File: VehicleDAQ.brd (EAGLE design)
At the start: 100 x 80 mm, 15 parts, among them IC1 786TV, IC3 78L05Z, X1 RASPI_BOARD_B+_FP

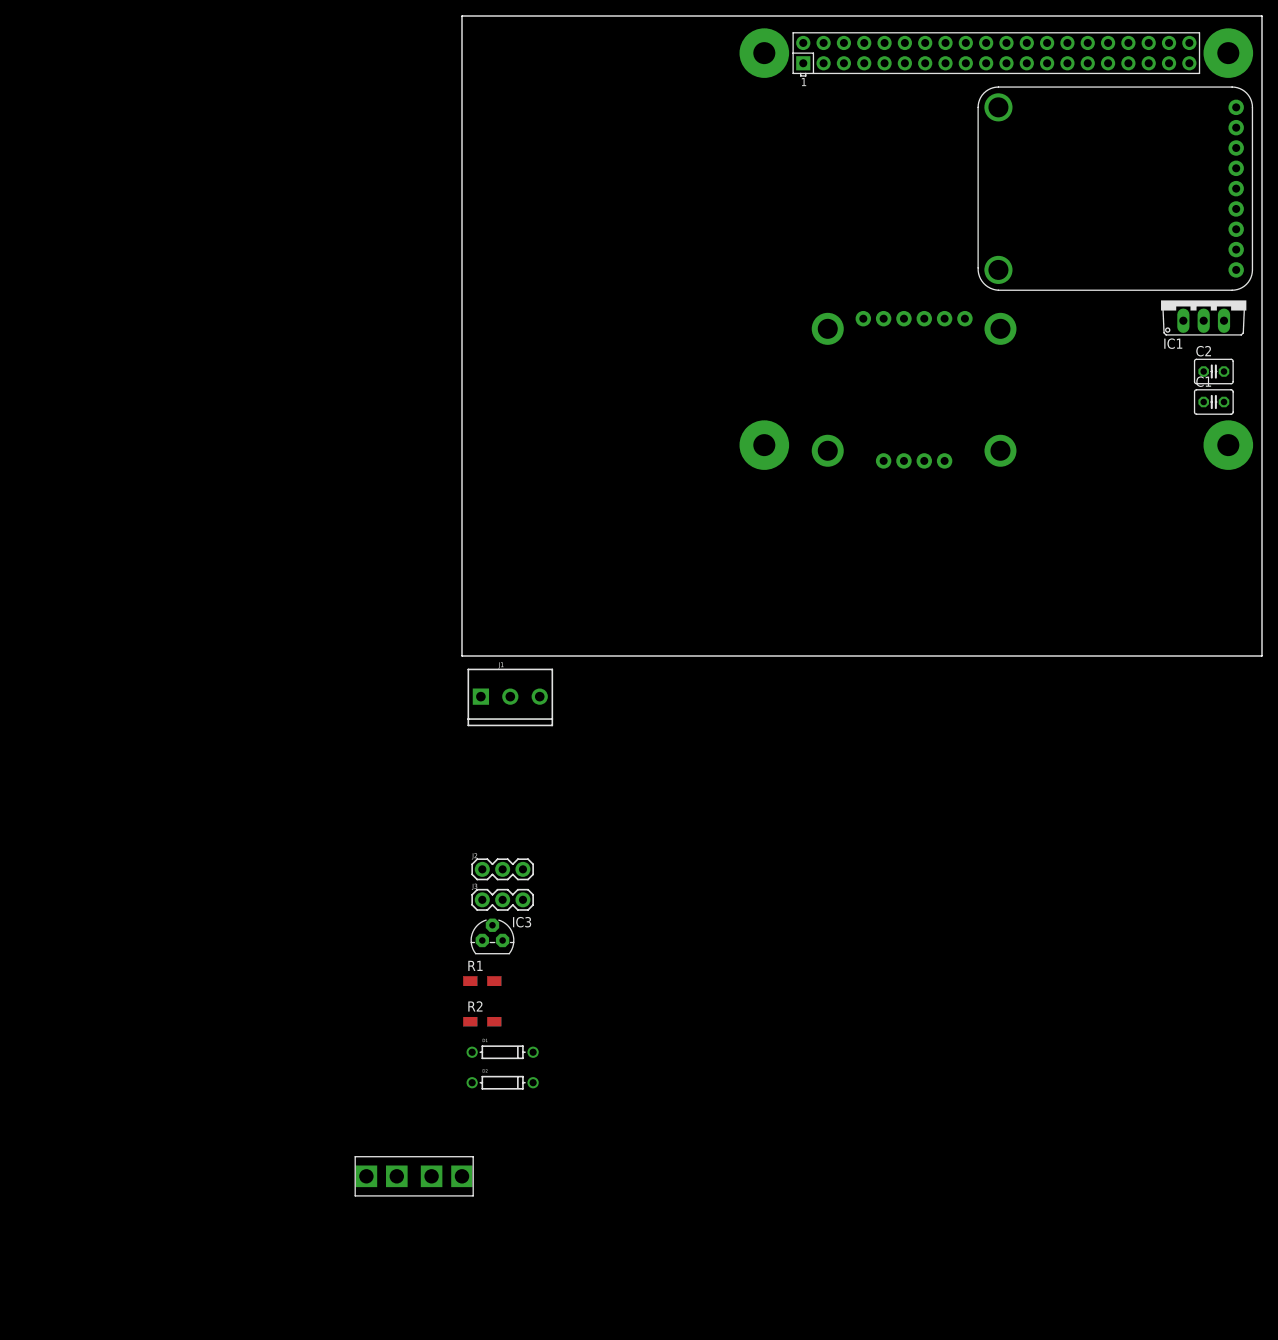
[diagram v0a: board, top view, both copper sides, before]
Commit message: Added actual regulators and capacitors.  All surface mount caps and regulators.
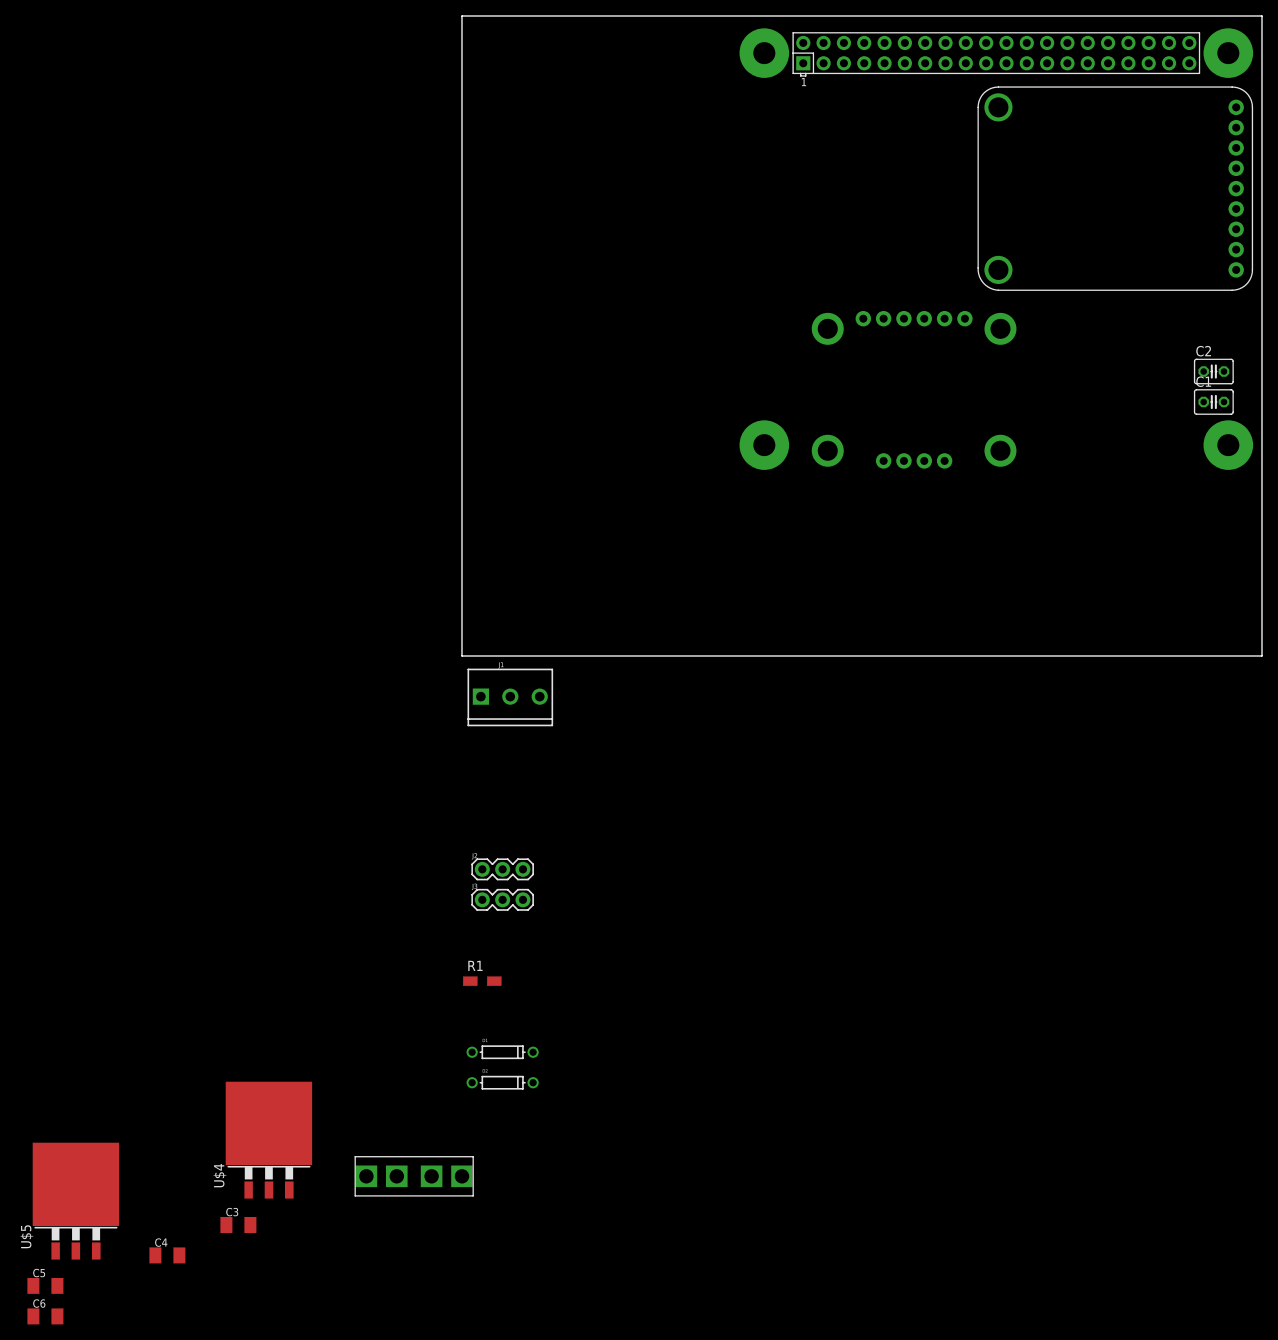
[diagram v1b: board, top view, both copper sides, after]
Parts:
- removed IC1: 786TV, linear:TO220V
- removed IC3: 78L05Z, adafruit:TO92
- removed R2: (no value), rcl:R1206W
- added C3, C4, C5, C6: (no value), adafruit:C1206K
- added U$4, U$5: LD1085D2M33R_REGULATOR, keverly:TO263-3
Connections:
- net +5V: now also C6.1, U$5.2, U$5.TAB; no longer IC1.3
- net GND: now also C3.2, C4.2, C5.2, C6.2, U$4.1, U$5.1; no longer IC1.2, IC3.2, R2.2
- net GPS_BATT_PWR: now also C4.1, U$4.2, U$4.TAB; no longer IC3.1
- net N$1: no longer R2.1
- net PWR_KEEP_ALIVE: now also X1.29; no longer X1.16
- net RELAY_NO: now also C5.1, U$5.3; no longer IC1.1
- net RELAY_PWR_IN: now also C3.1, U$4.3; no longer IC3.3
